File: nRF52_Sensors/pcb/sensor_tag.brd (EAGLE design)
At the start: 36.5 x 26.7 mm, 5 parts

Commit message: nRF52 tests ongoing
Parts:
- added U$6: CR2477, cr2477:CR2477
- moved U$5 1.27 mm to (25.4, 2.54)
- turned U$4 to 180 degrees
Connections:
- new net RX: U$3.P0_07, U$5.RX
- net GND: now also U$6.GND
- net SWCLK: now also U$5.SWDCLK; no longer U$5.SWCLK
- net VCC: now also U$6.VCC
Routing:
- net GND: track 51.8 -> 7.72 mm
- net INT: track 25.6 -> 33.8 mm, vias 0 -> 1
- net RX: track 0.00 -> 7.40 mm
- net SCL: track 31.2 -> 37.8 mm, vias 0 -> 1
- net VCC: track 77.1 -> 83.6 mm, vias 2 -> 3
- net SDA: track 31.2 -> 34.3 mm, vias 0 -> 1
- net TX: track 5.08 -> 7.40 mm
- net SWCLK: track 17.8 -> 18.8 mm
- net SWDIO: track 21.4 -> 22.4 mm

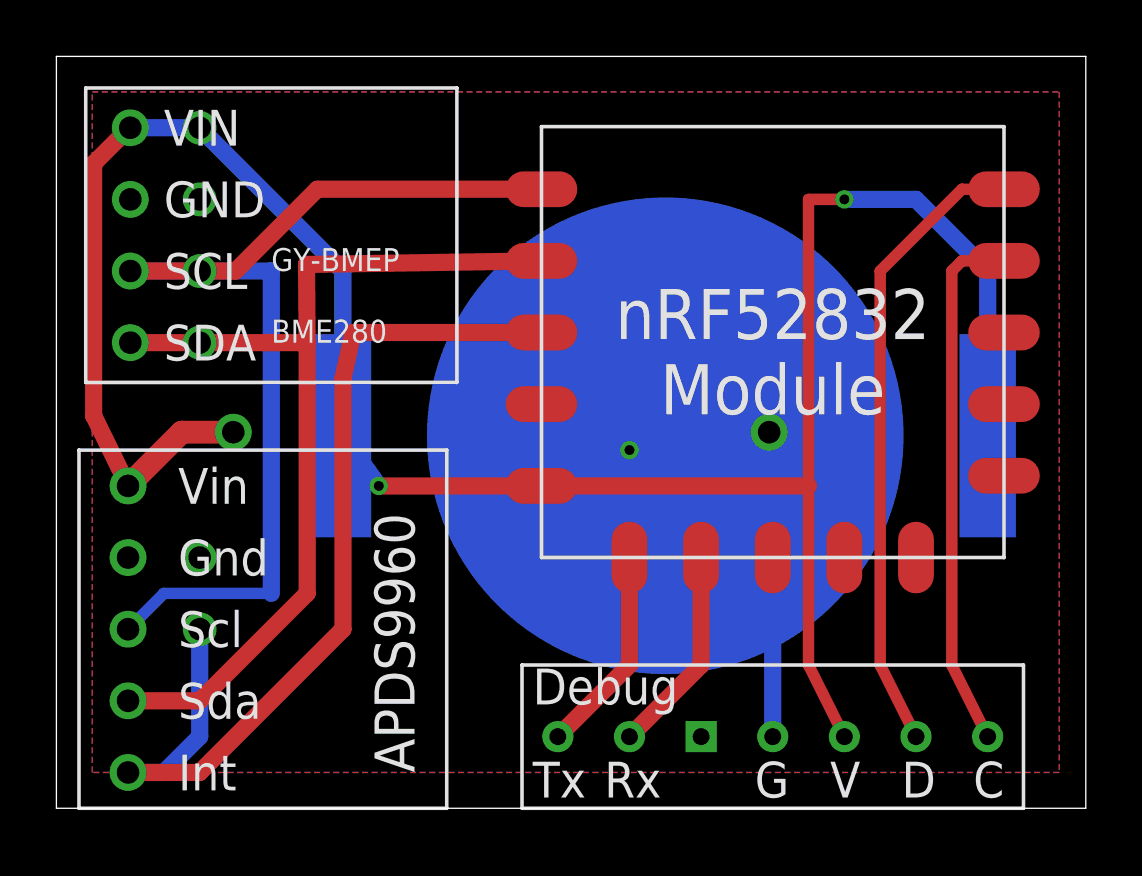
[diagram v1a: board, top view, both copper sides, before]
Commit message: fixed board design issues and zip gerber of new order
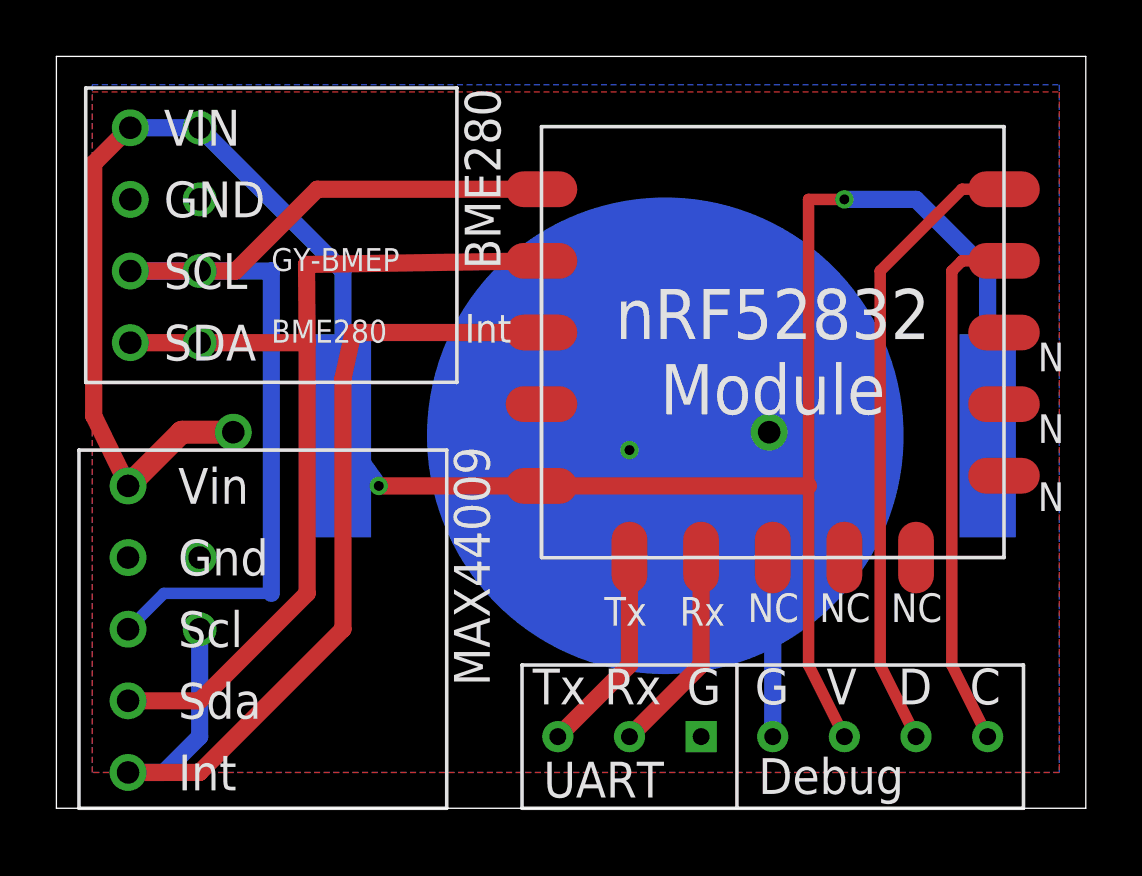
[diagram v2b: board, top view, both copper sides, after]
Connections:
- net GND: now also U$5.GND1
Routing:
- net GND: vias 2 -> 3
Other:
- board text added: "BME280"
- board text added: "Int"
- board text added: "MAX44009"
- board text added: "N"
- board text added: "NC"
- board text added: "Rx"
- board text added: "Tx"
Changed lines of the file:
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@@
 <layer number="1" name="Top" color="4" fill="1" visible="yes" active="yes"/>
 <layer number="16" name="Bottom" color="1" fill="1" visible="yes" active="yes"/>
-<layer number="17" name="Pads" color="2" fill="1" visible="yes" active="yes"/>
-<layer number="18" name="Vias" color="2" fill="1" visible="yes" active="yes"/>
+<layer number="17" name="Pads" color="2" fill="1" visible="no" active="yes"/>
+<layer number="18" name="Vias" color="2" fill="1" visible="no" active="yes"/>
 <layer number="19" name="Unrouted" color="6" fill="1" visible="yes" active="yes"/>
 <layer number="20" name="Dimension" color="24" fill="1" visible="yes" active="yes"/>
 <layer number="21" name="tPlace" color="7" fill="1" visible="yes" active="yes"/>
-<layer number="22" name="bPlace" color="7" fill="1" visible="yes" active="yes"/>
-<layer number="23" name="tOrigins" color="15" fill="1" visible="yes" active="yes"/>
-<layer number="24" name="bOrigins" color="15" fill="1" visible="yes" active="yes"/>
-<layer number="25" name="tNames" color="7" fill="1" visible="yes" active="yes"/>
-<layer number="26" name="bNames" color="7" fill="1" visible="yes" active="yes"/>
-<layer number="27" name="tValues" color="7" fill="1" visible="yes" active="yes"/>
+<layer number="22" name="bPlace" color="7" fill="1" visible="no" active="yes"/>
+<layer number="23" name="tOrigins" color="15" fill="1" visible="no" active="yes"/>
+<layer number="24" name="bOrigins" color="15" fill="1" visible="no" active="yes"/>
+<layer number="25" name="tNames" color="7" fill="1" visible="no" active="yes"/>
+<layer number="26" name="bNames" color="7" fill="1" visible="no" active="yes"/>
+<layer number="27" name="tValues" color="7" fill="1" visible="no" active="yes"/>
 <layer number="28" name="bValues" color="7" fill="1" visible="yes" active="yes"/>
 <layer number="29" name="tStop" color="7" fill="3" visible="no" active="yes"/>
@@
 <wire x1="36.5" y1="26.66" x2="0" y2="26.66" width="0" layer="20"/>
 <wire x1="0" y1="26.66" x2="0" y2="0" width="0" layer="20"/>
+<text x="24.511" y="6.604" size="1.016" layer="21">NC</text>
+<text x="27.051" y="6.604" size="1.016" layer="21">NC</text>
+<text x="29.591" y="6.604" size="1.016" layer="21">NC</text>
+<text x="34.798" y="15.494" size="1.016" layer="21">N</text>
+<text x="34.798" y="12.954" size="1.016" layer="21">N</text>
+<text x="34.798" y="10.541" size="1.016" layer="21">N</text>
+<text x="19.431" y="6.477" size="1.016" layer="21">Tx</text>
+<text x="22.098" y="6.477" size="1.016" layer="21">Rx</text>
+<text x="14.478" y="16.51" size="1.016" layer="21">Int</text>
+<text x="14.097" y="12.827" size="1.27" layer="21" rot="R270">MAX44009</text>
+<text x="14.478" y="25.527" size="1.27" layer="21" rot="R270">BME280</text>
 </plain>
 <attributes>
@@
 <vertex x="1.27" y="1.27"/>
 </polygon>
-<polygon width="0.4572" layer="16" isolate="0.4572">
-<vertex x="1.27" y="25.4"/>
-<vertex x="35.56" y="25.4"/>
+<polygon width="0.4572" layer="16" isolate="0.4064">
+<vertex x="1.27" y="25.654"/>
+<vertex x="35.56" y="25.654"/>
 <vertex x="35.56" y="1.27"/>
 <vertex x="1.27" y="1.27"/>
@@
 <contactref element="U$6" pad="GND"/>
 <via x="20.32" y="12.7" extent="1-16" drill="0.35"/>
+<via x="5.08" y="21.59" extent="1-16" drill="0.8"/>
+<contactref element="U$5" pad="GND1"/>
 </signal>
 <signal name="VCC">
@@
 <wire x1="22.86" y1="5.08" x2="22.86" y2="8.89" width="0.6096" layer="1"/>
 </signal>
-<signal name="N$1">
-<via x="5.08" y="21.59" extent="1-16" drill="0.8"/>
-</signal>
 </signals>
